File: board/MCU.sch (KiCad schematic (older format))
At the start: 15 parts, among them J1 ICSP, U1 PIC16F15345-IP, U2 MAX232I, Y1 8MHz

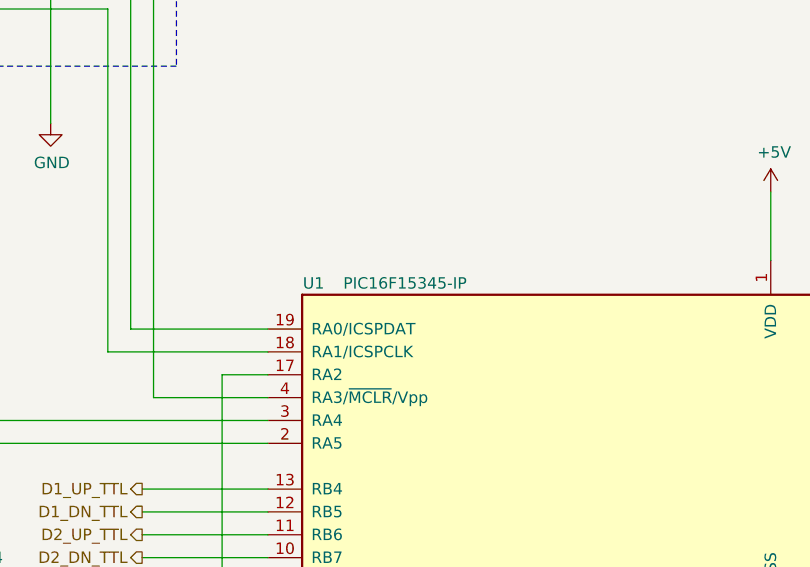
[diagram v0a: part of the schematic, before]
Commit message: Add/correct a bunch of part numbers
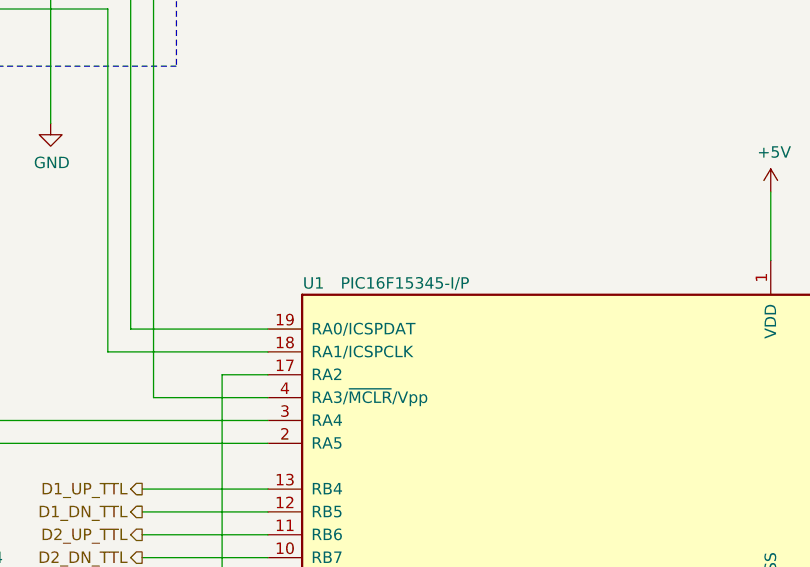
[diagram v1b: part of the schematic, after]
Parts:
- U1: value PIC16F15345-IP -> PIC16F15345-I/P; Src1 (none) -> Mouser; Src1 Part (none) -> 579-PIC16F15345-I/P; Src1 URL (none) -> https://www.mouser.com/ProductDetail/579-PIC16F15345-I-P; mfr (none) -> Microchip; mpn (none) -> PIC16F15345-I/P
- U2: Src1 (none) -> Mouser; Src1 Part (none) -> 595-MAX232IN; Src1 URL (none) -> https://www.mouser.com/ProductDetail/595-MAX232IN; mfr (none) -> TI; mpn (none) -> MAX232IN
- Y1: Src1 (none) -> Mouser; Src1 Part (none) -> 73-XT49S800-20; Src1 URL (none) -> https://www.mouser.com/ProductDetail/73-XT49S800-20; mfr (none) -> Vishay; mpn (none) -> XT9S20ANA8M
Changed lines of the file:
@@
 F 2 "Package_DIP:DIP-16_W7.62mm_LongPads" H 9250 2850 50  0001 L CNN
 F 3 "http://www.ti.com/lit/ds/symlink/max232.pdf" H 9200 4000 50  0001 C CNN
+F 4 "TI" H 9200 3900 50  0001 C CNN "mfr"
+F 5 "MAX232IN" H 9200 3900 50  0001 C CNN "mpn"
+F 6 "Mouser" H 9200 3900 50  0001 C CNN "Src1"
+F 7 "595-MAX232IN" H 9200 3900 50  0001 C CNN "Src1 Part"
+F 8 "https://www.mouser.com/ProductDetail/595-MAX232IN" H 9200 3900 50  0001 C CNN "Src1 URL"
 	1    9200 3900
 	1    0    0    -1
@@
 F 1 "8MHz" H 1000 4427 50  0000 C CNN
 F 2 "Crystal:Crystal_HC49-4H_Vertical" H 1000 4250 50  0001 C CNN
-F 3 "~" H 1000 4250 50  0001 C CNN
+F 3 "https://www.mouser.com/datasheet/2/427/xt49s-88235.pdf" H 1000 4250 50  0001 C CNN
+F 4 "Vishay" H 1000 4250 50  0001 C CNN "mfr"
+F 5 "XT9S20ANA8M" H 1000 4250 50  0001 C CNN "mpn"
+F 6 "Mouser" H 1000 4250 50  0001 C CNN "Src1"
+F 7 "73-XT49S800-20" H 1000 4250 50  0001 C CNN "Src1 Part"
+F 8 "https://www.mouser.com/ProductDetail/73-XT49S800-20" H 1000 4250 50  0001 C CNN "Src1 URL"
 	1    1000 4250
 	1    0    0    -1
@@
 P 4700 4000
 F 0 "U1" H 2700 4700 50  0000 C CNN
-F 1 "PIC16F15345-IP" H 3100 4700 50  0000 C CNN
+F 1 "PIC16F15345-I/P" H 3100 4700 50  0000 C CNN
 F 2 "Package_DIP:DIP-20_W7.62mm_LongPads" H 4700 4000 50  0001 C CNN
 F 3 "http://ww1.microchip.com/downloads/en/DeviceDoc/40001865B.pdf" H 4700 4000 50  0001 C CNN
+F 4 "Microchip" H 4700 4000 50  0001 C CNN "mfr"
+F 5 "PIC16F15345-I/P" H 4700 4000 50  0001 C CNN "mpn"
+F 6 "Mouser" H 4700 4000 50  0001 C CNN "Src1"
+F 7 "579-PIC16F15345-I/P" H 4700 4000 50  0001 C CNN "Src1 Part"
+F 8 "https://www.mouser.com/ProductDetail/579-PIC16F15345-I-P" H 4700 4000 50  0001 C CNN "Src1 URL"
 	1    4700 4000
 	1    0    0    -1

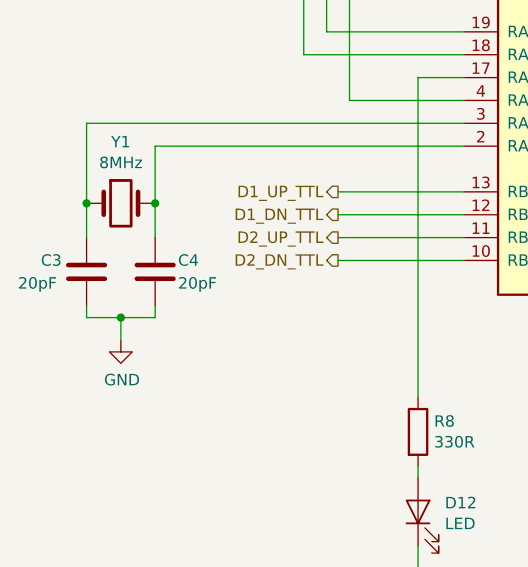
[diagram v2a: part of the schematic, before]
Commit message: Update xtal load capacitors, fix left mounting holes
* Try some 33pF caps for the crystal.
* Reflect the left side mounting holes in the schematic.
* Reroute one RS232 TTL line; though now more stuff runs under the clock
  lines so may move all the RS232 TTL traces later.
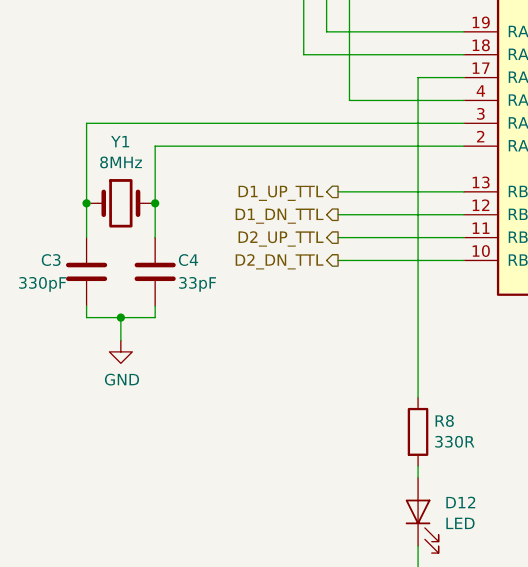
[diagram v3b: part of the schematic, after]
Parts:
- C3: value 20pF -> 330pF; Src1 (none) -> Mouser; Src1 Part (none) -> 810-FG18C0G1H330JNT6; Src1 URL (none) -> https://www.mouser.com/ProductDetail/810-FG18C0G1H330JNT6; mfr (none) -> TDK; mpn (none) -> FG18C0G1H330JNT06
- C4: value 20pF -> 33pF; Src1 (none) -> Mouser; Src1 Part (none) -> 810-FG18C0G1H330JNT6; Src1 URL (none) -> https://www.mouser.com/ProductDetail/810-FG18C0G1H330JNT6; mfr (none) -> TDK; mpn (none) -> FG18C0G1H330JNT06
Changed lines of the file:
@@
 Sheet 2 4
 Title "Projector Screen Controller"
-Date "2019-09-21"
+Date "2019-09-22"
 Rev "0.2"
 Comp "Flirble Open Source"
@@
 P 850 4550
 F 0 "C3" H 650 4600 50  0000 L CNN
-F 1 "20pF" H 550 4500 50  0000 L CNN
+F 1 "330pF" H 550 4500 50  0000 L CNN
 F 2 "Capacitor_THT:C_Disc_D5.0mm_W2.5mm_P2.50mm" H 888 4400 50  0001 C CNN
-F 3 "~" H 850 4550 50  0001 C CNN
+F 3 "https://www.mouser.com/datasheet/2/400/eadmlcc_halogenfree_fg_en-775693.pdf" H 850 4550 50  0001 C CNN
+F 4 "TDK" H 850 4550 50  0001 C CNN "mfr"
+F 5 "FG18C0G1H330JNT06" H 850 4550 50  0001 C CNN "mpn"
+F 6 "Mouser" H 850 4550 50  0001 C CNN "Src1"
+F 7 "810-FG18C0G1H330JNT6" H 850 4550 50  0001 C CNN "Src1 Part"
+F 8 "https://www.mouser.com/ProductDetail/810-FG18C0G1H330JNT6" H 850 4550 50  0001 C CNN "Src1 URL"
 	1    850  4550
 	1    0    0    -1
@@
 P 1150 4550
 F 0 "C4" H 1250 4600 50  0000 L CNN
-F 1 "20pF" H 1250 4500 50  0000 L CNN
+F 1 "33pF" H 1250 4500 50  0000 L CNN
 F 2 "Capacitor_THT:C_Disc_D5.0mm_W2.5mm_P2.50mm" H 1188 4400 50  0001 C CNN
-F 3 "~" H 1150 4550 50  0001 C CNN
+F 3 "https://www.mouser.com/datasheet/2/400/eadmlcc_halogenfree_fg_en-775693.pdf" H 1150 4550 50  0001 C CNN
+F 4 "TDK" H 1150 4550 50  0001 C CNN "mfr"
+F 5 "FG18C0G1H330JNT06" H 1150 4550 50  0001 C CNN "mpn"
+F 6 "Mouser" H 1150 4550 50  0001 C CNN "Src1"
+F 7 "810-FG18C0G1H330JNT6" H 1150 4550 50  0001 C CNN "Src1 Part"
+F 8 "https://www.mouser.com/ProductDetail/810-FG18C0G1H330JNT6" H 1150 4550 50  0001 C CNN "Src1 URL"
 	1    1150 4550
 	1    0    0    -1

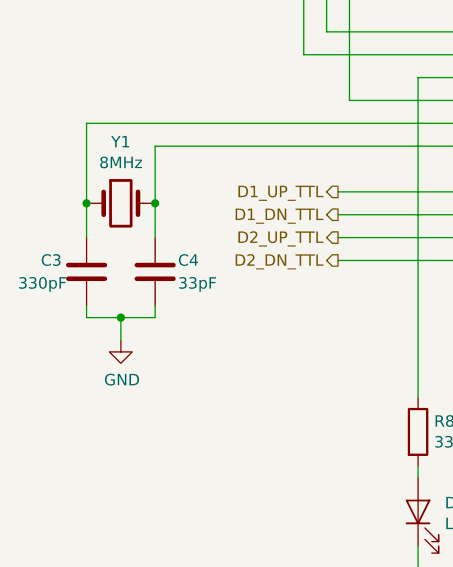
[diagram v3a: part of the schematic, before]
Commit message: Make room for input filtering
* Move the crystal block up and isolate its ground plane.
* Route the RS232 TTL signals around the crystal block.
* Update images, PDFs and gerbers.
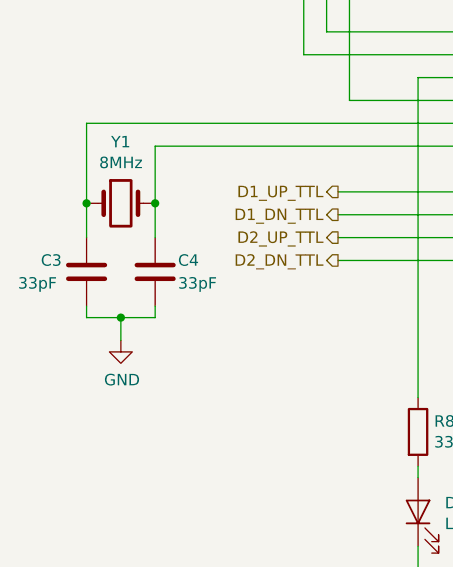
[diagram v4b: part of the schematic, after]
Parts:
- C3: value 330pF -> 33pF
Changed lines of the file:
@@
 P 850 4550
 F 0 "C3" H 650 4600 50  0000 L CNN
-F 1 "330pF" H 550 4500 50  0000 L CNN
+F 1 "33pF" H 550 4500 50  0000 L CNN
 F 2 "Capacitor_THT:C_Disc_D5.0mm_W2.5mm_P2.50mm" H 888 4400 50  0001 C CNN
 F 3 "https://www.mouser.com/datasheet/2/400/eadmlcc_halogenfree_fg_en-775693.pdf" H 850 4550 50  0001 C CNN

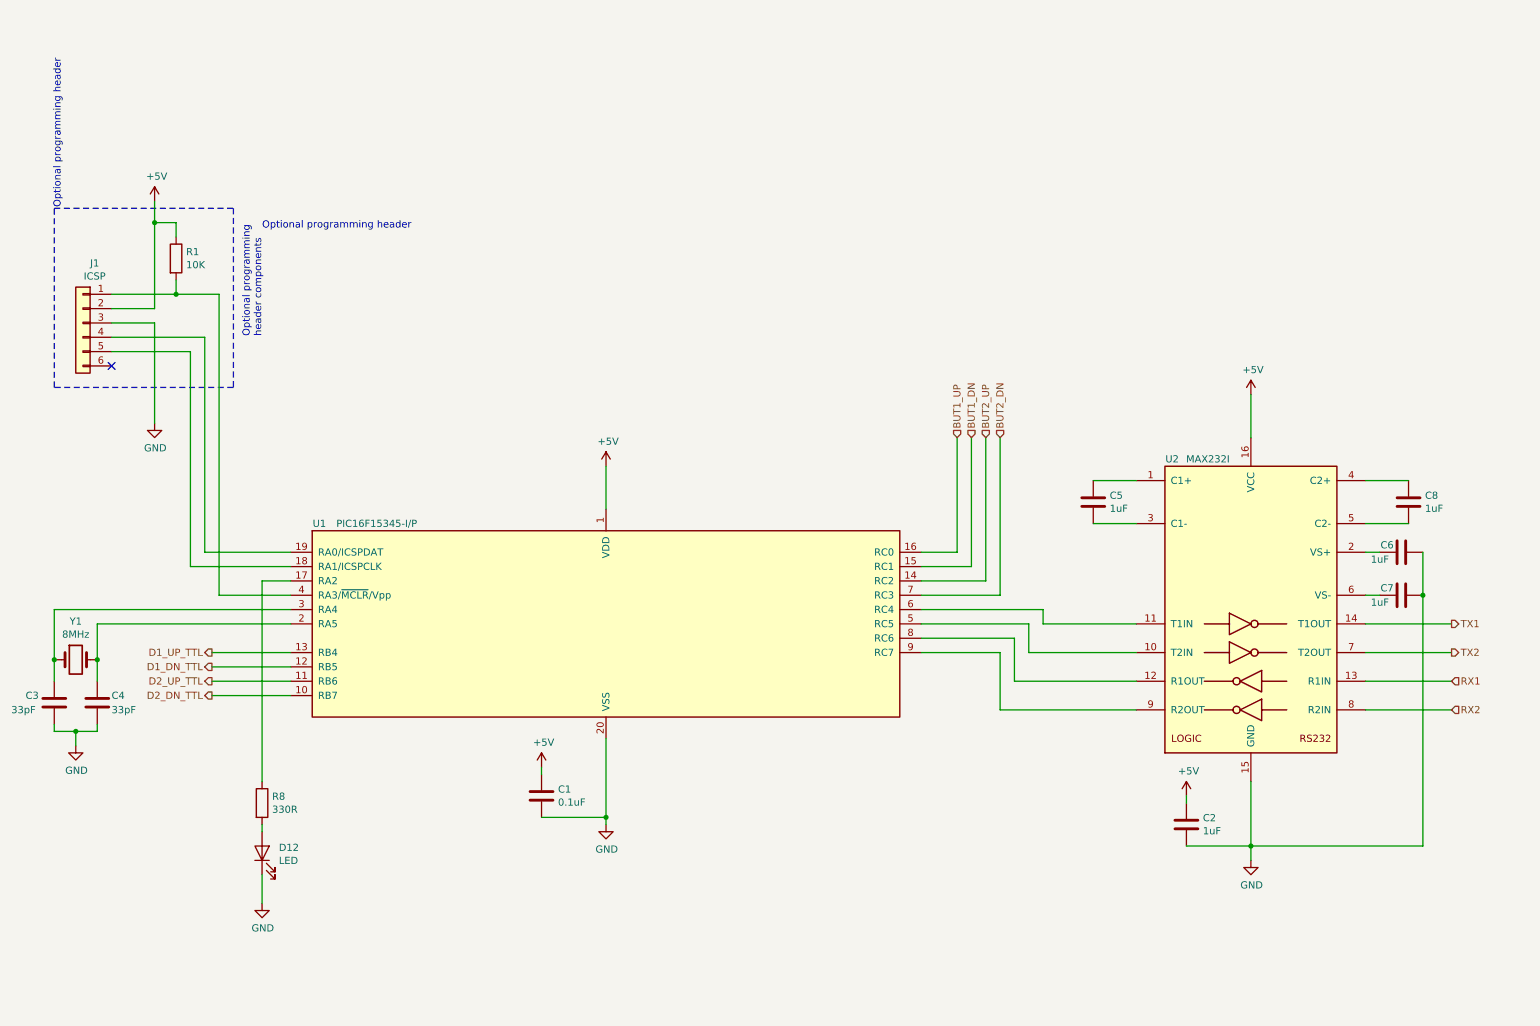
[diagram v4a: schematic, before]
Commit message: First pass at input protection for buttons
* Schottky diodes & capacitors to limit and smooth the inputs.
* Relies on the WPU of the MCU to provide a charge for the C (possibly
  a bad idea, will see).
* Had to move a bunch of stuff to make room and make sure the ground paths
  were sensible.
* Update all the disc capacitors to the Kicad 5 footprint.
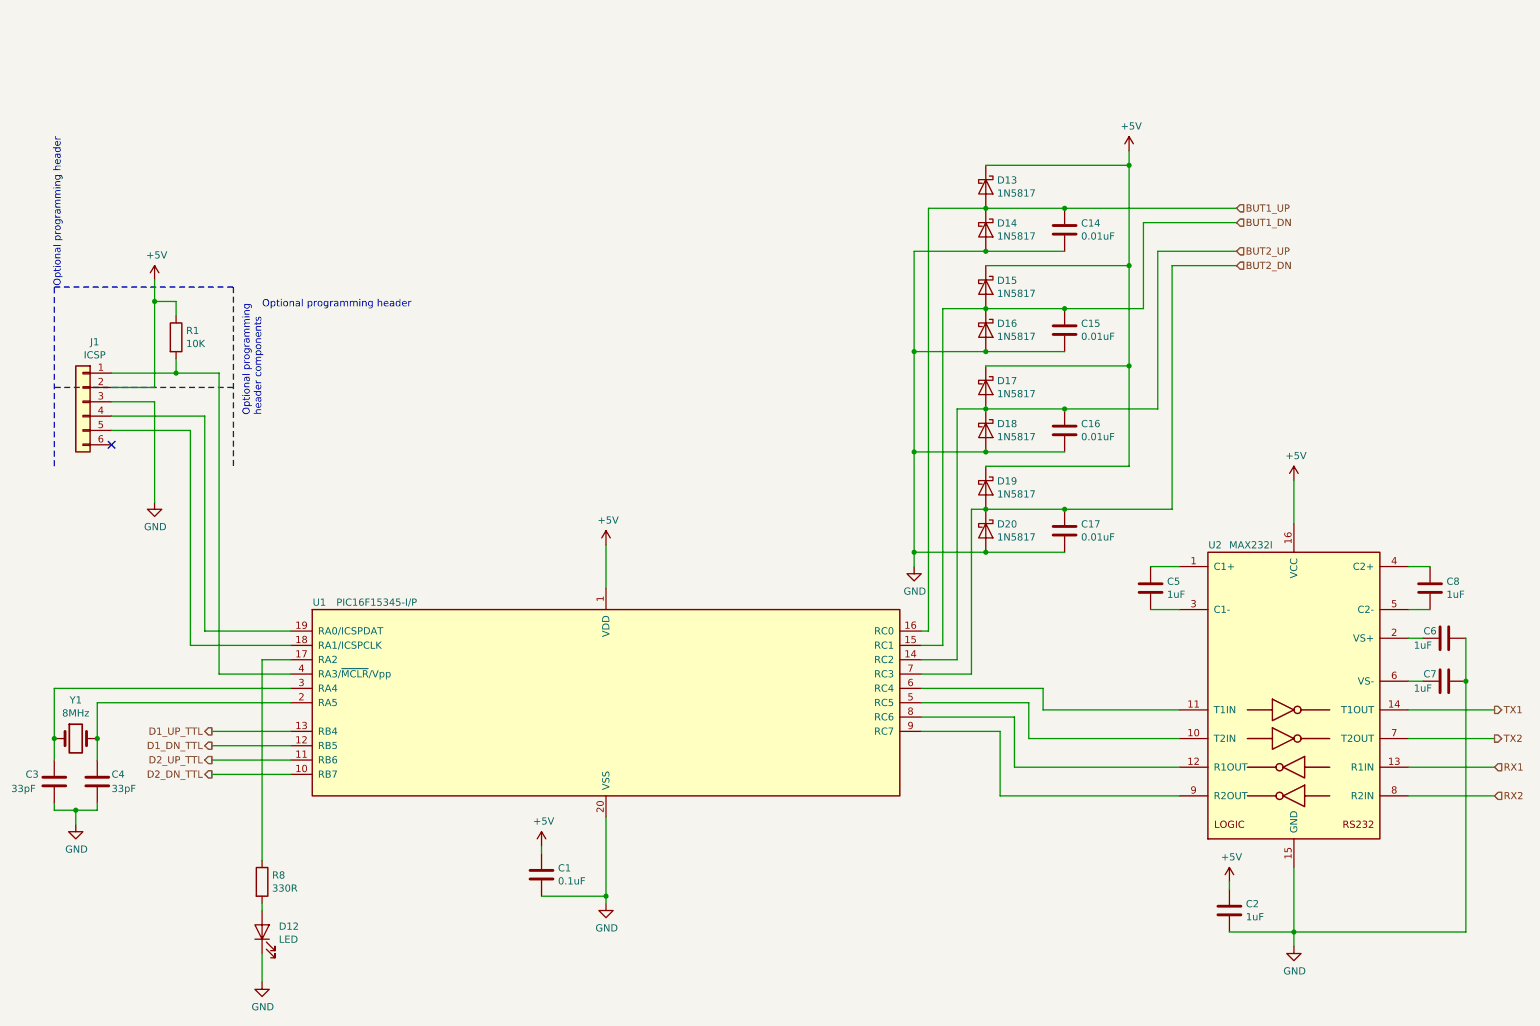
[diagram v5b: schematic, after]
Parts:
- added C14, C15, C16, C17: 0.01uF, Capacitors_THT:C_Disc_D5.0mm_W2.5mm_P2.50mm, symbol Device:C
- added D13, D14, D15, D16, D17, D18, D19, D20: 1N5817, Diodes_THT:D_DO-41_SOD81_P2.54mm_Vertical_KathodeUp, symbol Device:D_Schottky
- C1, C2, C3, C4, C5, C6, C7, C8: footprint Capacitor_THT:C_Disc_D5.0mm_W2.5mm_P2.50mm -> Capacitors_THT:C_Disc_D5.0mm_W2.5mm_P2.50mm
- D12: footprint LED_THT:LED_D3.0mm -> LEDs:LED_D3.0mm
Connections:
- net +5V: now also D13.1 (K), D15.1 (K), D17.1 (K), D19.1 (K)
- net BUT1_DN: now also C15.1, D15.2 (A), D16.1 (K)
- net BUT1_UP: now also C14.1, D13.2 (A), D14.1 (K)
- net BUT2_DN: now also C17.1, D19.2 (A), D20.1 (K)
- net BUT2_UP: now also C16.1, D17.2 (A), D18.1 (K)
- net GND: now also C14.2, C15.2, C16.2, C17.2, D14.2 (A), D16.2 (A), D18.2 (A), D20.2 (A)
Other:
- moved on the sheet: C1, C2, C3, C4, C5, C6, C7, C8, D12, J1, R1, R8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
